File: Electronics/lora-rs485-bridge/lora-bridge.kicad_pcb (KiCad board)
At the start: 2 copper layers, 53 x 94 mm, 39 parts, among them J1 battery, J2 ANT, J3 i2c, J4 rs485, J9 USB micro, Q7 Q_PMOS_GSD, SW1 SW_Test, SW2 SW_Reset, U1 SN65HVD72, U2 ATSAMD21G18A-AUT, U3 RFM95W-868S2, U4 MCP1810T-33I_OT, Y1 32.768

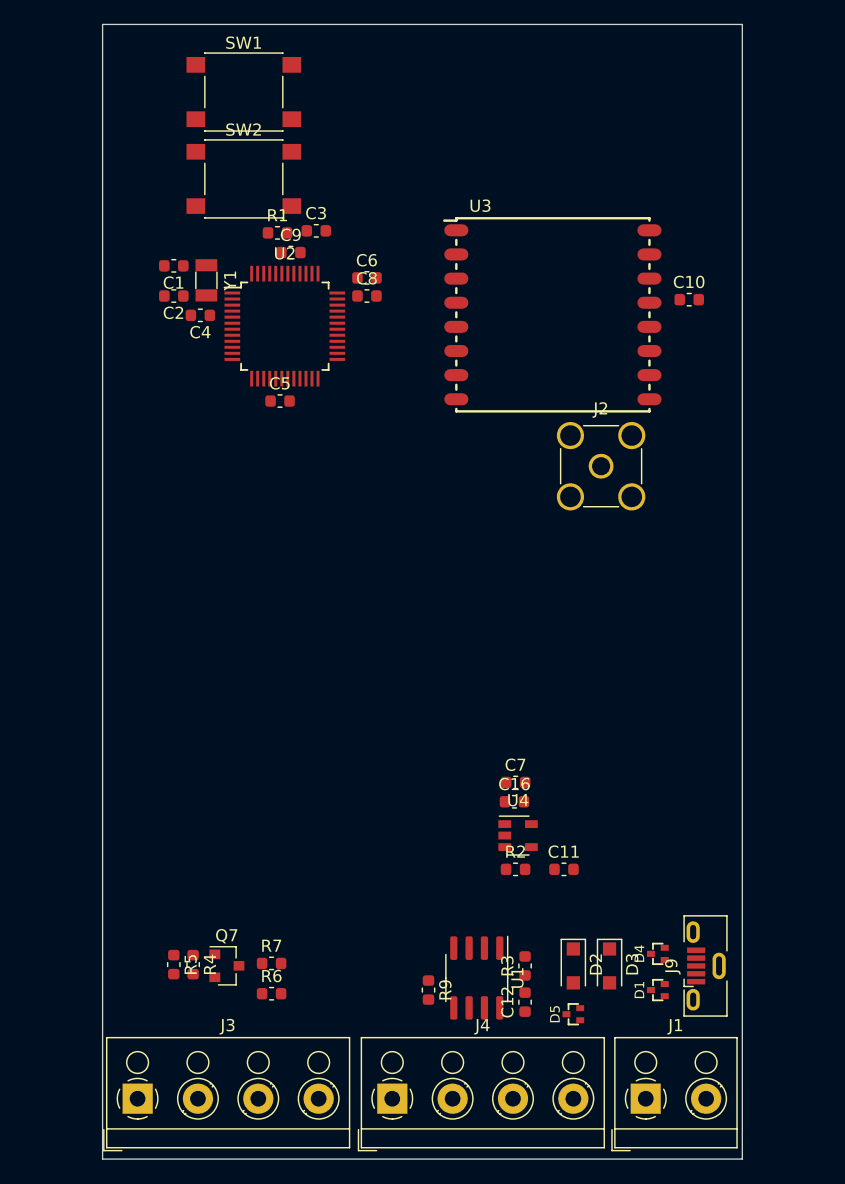
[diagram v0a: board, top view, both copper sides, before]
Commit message: Add ESD protection to i2c lines, change VIN TVS diode to higher voltage, add series resistors to SPI lines, compress the PCB to be at width of typical 4xAA battery holder
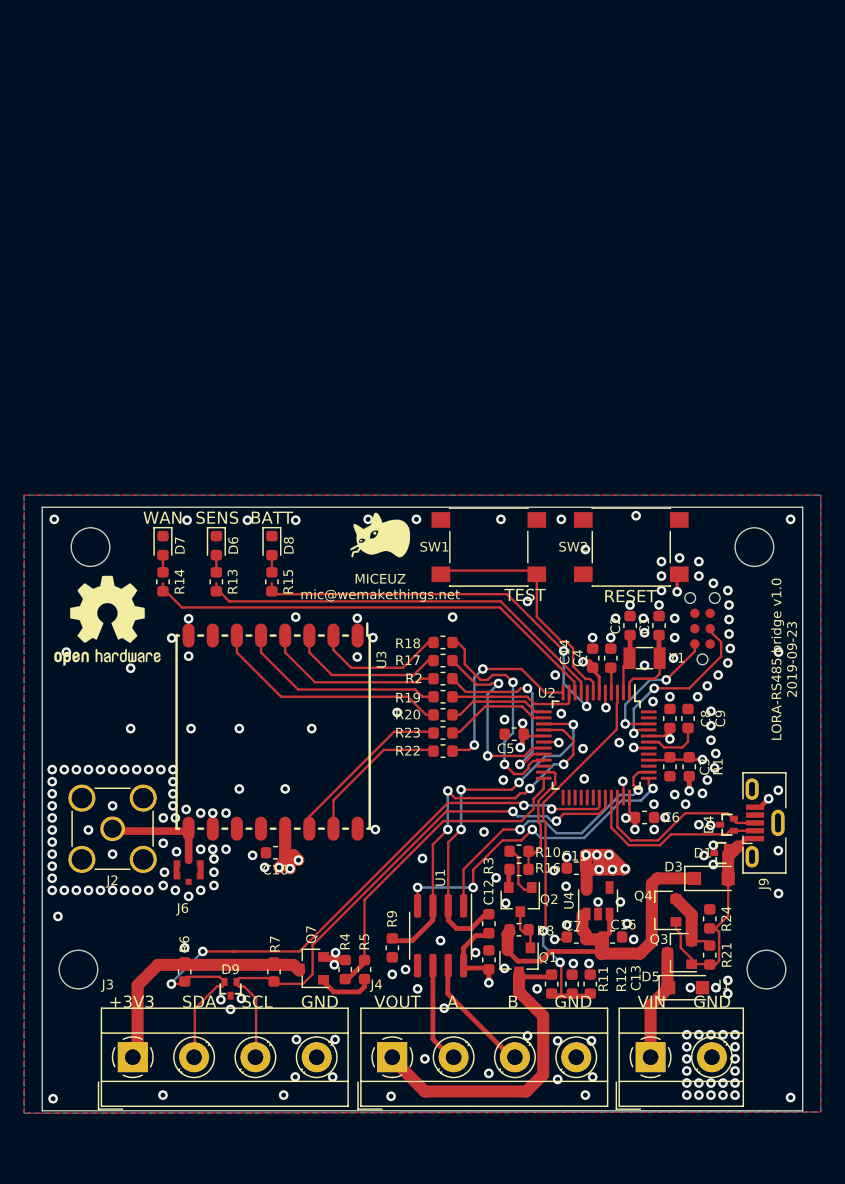
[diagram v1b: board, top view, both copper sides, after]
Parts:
- removed D2: D_Schottky, Diode_SMD:D_SOD-123F
- added C13: 1u, Capacitor_SMD:C_0603_1608Metric, F.Cu at (130.4, 132.5)
- added C14: 1u, Capacitor_SMD:C_0603_1608Metric, F.Cu at (130.6, 105.5)
- added D6: LED, LED_SMD:LED_0603_1608Metric, F.Cu at (99.4, 96.2)
- added D7: LED, LED_SMD:LED_0603_1608Metric, F.Cu at (95.0, 96.2)
- added D8: LED, LED_SMD:LED_0603_1608Metric, F.Cu at (104.0, 96.2)
- added D9: D_TVS_x2_AAC, miceuz-lib:SC89, F.Cu at (100.6, 132.9)
- added G***: LOGO, miceuz-lib:catnip, F.Cu at (113.0, 95.3)
- added H1: MountingHole, Mounting_Holes:MountingHole_3.2mm_M3_DIN965, F.Cu at (144.0, 96.3)
- added H2: MountingHole, Mounting_Holes:MountingHole_3.2mm_M3_DIN965, F.Cu at (145.0, 131.3)
- added H3: MountingHole, Mounting_Holes:MountingHole_3.2mm_M3_DIN965, F.Cu at (89.0, 96.3)
- added H4: MountingHole, Mounting_Holes:MountingHole_3.2mm_M3_DIN965, F.Cu at (88.0, 131.3)
- added J5: SWD, miceuz-lib:TC2030-MCP-NL, F.Cu at (139.7, 105.6)
- added J6: ANT, miceuz-lib:U.FL_TEConnectivity_2334884_1, F.Cu at (97.1, 123.0)
- added Q1: Q_PMOS_GSD, Package_TO_SOT_SMD:SOT-23, F.Cu at (124.5, 130.5)
- added Q2: Q_NMOS_GSD, Package_TO_SOT_SMD:SOT-23, F.Cu at (124.6, 125.5)
- added Q3: Q_PMOS_GSD, Package_TO_SOT_SMD:SOT-23, F.Cu at (137.8, 129.9)
- added Q4: Q_PMOS_GSD, Package_TO_SOT_SMD:SOT-23, F.Cu at (136.5, 126.4)
- added R10: 150, Resistor_SMD:R_0603_1608Metric, F.Cu at (124.5, 121.5)
- added R11: 10k, Resistor_SMD:R_0603_1608Metric, F.Cu at (127.2, 132.5)
- added R12: 10k, Resistor_SMD:R_0603_1608Metric, F.Cu at (128.9, 132.5)
- added R13: 10k, Resistor_SMD:R_0603_1608Metric, F.Cu at (99.4, 99.2)
- added R14: 10k, Resistor_SMD:R_0603_1608Metric, F.Cu at (95.0, 99.2)
- added R15: 10k, Resistor_SMD:R_0603_1608Metric, F.Cu at (104.0, 99.2)
- added R16: 1M, Resistor_SMD:R_0603_1608Metric, F.Cu at (124.5, 123.0)
- added R17: 150, Resistor_SMD:R_0603_1608Metric, F.Cu at (118.2, 105.7)
- added R18: 150, Resistor_SMD:R_0603_1608Metric, F.Cu at (118.2, 104.2)
- added R19: 150, Resistor_SMD:R_0603_1608Metric, F.Cu at (118.2, 108.7)
- added R20: 150, Resistor_SMD:R_0603_1608Metric, F.Cu at (118.2, 110.2)
- added R21: 1M, Resistor_SMD:R_0603_1608Metric, F.Cu at (140.3, 130.1)
- added R22: 150, Resistor_SMD:R_0603_1608Metric, F.Cu at (118.2, 113.2)
- added R23: 150, Resistor_SMD:R_0603_1608Metric, F.Cu at (118.2, 111.7)
- added R24: 150, Resistor_SMD:R_0603_1608Metric, F.Cu at (140.3, 127.1)
- added R8: 1M, Resistor_SMD:R_0603_1608Metric, F.Cu at (124.5, 128.0)
- added REF***: OSHW-Logo2_9.8x8mm_SilkScreen, Symbols:OSHW-Logo2_9.8x8mm_SilkScreen, F.Cu at (90.4, 102.4)
- D5: value D_TVS_x2_AAC -> D_TVS; footprint miceuz-lib:SC89 -> Diode_SMD:D_SOD-123F
- J1: footprint TerminalBlock_RND:TerminalBlock_RND_205-00001_Pitch5.00mm -> TerminalBlock_MetzConnect:TerminalBlock_MetzConnect_Type101_RT01602HBWC_Pitch5.08mm
- J3, J4: footprint TerminalBlock_RND:TerminalBlock_RND_205-00003_Pitch5.00mm -> TerminalBlock_MetzConnect:TerminalBlock_MetzConnect_Type101_RT01604HBWC_Pitch5.08mm
- R2: value 0 -> 150
- U4: value MCP1810T-33I_OT -> NCP718; footprint Package_TO_SOT_SMD:SOT-23-5 -> TO_SOT_Packages_SMD:SOT-23-5
- moved C10 57.2 mm to (104.3, 121.6), turned to 180 degrees
- moved R1 55.9 mm to (138.6, 114.5), turned to 90 degrees
- moved C3 53.2 mm to (137.0, 114.5), turned to -90 degrees
- moved C9 50.7 mm to (138.5, 110.5), turned to 90 degrees
- moved J2 50.4 mm to (90.8, 119.6), turned to -90 degrees
- moved C6 50.3 mm to (134.9, 118.7)
- moved C1 50.0 mm to (136.1, 102.8), turned to 90 degrees
- moved Y1 47.9 mm to (134.9, 105.5), turned to 180 degrees
- moved C2 46.6 mm to (133.7, 102.8), turned to 90 degrees
- moved C4 44.3 mm to (132.1, 105.5), turned to 90 degrees
- moved SW2 44.3 mm to (133.8, 96.3)
- moved U2 43.2 mm to (130.9, 112.7), turned to -90 degrees
- moved C8 43.1 mm to (137.0, 110.5), turned to 90 degrees
- moved SW1 42.8 mm to (122.0, 96.3)
- moved U3 34.6 mm to (111.1, 103.6), turned to -90 degrees
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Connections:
- C11 pad 1: Net-(C11-Pad1) -> +3V3
- D5 pad 2: /VIN -> GND
- J2 pad 1: GND -> /ANTENNA
- J2 pad 2: /ANTENNA -> GND
- J3 pad 2: /SCL_OUT -> /I2C_SDA
- J3 pad 3: /SDA_OUT -> /I2C_SCL
- J4 pad 1: +BATT -> /VOUT_1
- R2 pad 1: +3V3 -> Net-(R2-Pad1)
- R2 pad 2: Net-(C11-Pad1) -> /RFM_SCK
- U2 pad 10: Net-(U2-Pad10) -> /LED2
- U2 pad 15: Net-(U2-Pad15) -> /~RS485_RE
- U2 pad 16: Net-(U2-Pad16) -> /RS485_DE
- U2 pad 23: Net-(U2-Pad23) -> /RS485_ENABLE
- U2 pad 24: Net-(U2-Pad24) -> /~I2C_ENABLE
- U2 pad 3: Net-(U2-Pad3) -> /BATT_MON
- U2 pad 7: Net-(U2-Pad7) -> Net-(SW1-Pad2)
- U2 pad 8: Net-(U2-Pad8) -> /LED3
- U2 pad 9: Net-(U2-Pad9) -> /LED1
- U3 pad 14: /RFM_IRQ -> Net-(R23-Pad2)
- U3 pad 15: /DIO01 -> Net-(R22-Pad2)
- U3 pad 2: /RFM_MISO -> Net-(R18-Pad1)
- U3 pad 3: /RFM_MOSI -> Net-(R17-Pad1)
- U3 pad 4: /RFM_SCK -> Net-(R2-Pad1)
- U3 pad 5: /RFM_NSS -> Net-(R19-Pad1)
- U3 pad 6: /RFM_RST -> Net-(R20-Pad1)
- U4 pad 2: +BATT -> GND
- U4 pad 3: +3V3 -> +BATT
- U4 pad 5: GND -> +3V3
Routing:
- net /I2C_SDA: track 0.00 -> 55.9 mm, vias 0 -> 4
- net /I2C_SCL: track 0.00 -> 47.6 mm, vias 0 -> 2
- net +3V3: track 0.00 -> 42.5 mm, vias 0 -> 19
- net /LED2: track 0.00 -> 38.6 mm
- net /LED1: track 0.00 -> 34.8 mm
- net /LED3: track 0.00 -> 33.3 mm, vias 0 -> 2
- net +BATT: track 0.00 -> 32.1 mm
- net /BATT_MON: track 0.00 -> 31.5 mm, vias 0 -> 2
- net /RS485_DE: track 0.00 -> 31.4 mm, vias 0 -> 4
- net /~RS485_RE: track 0.00 -> 30.2 mm, vias 0 -> 4
- net /~I2C_ENABLE: track 0.00 -> 27.5 mm
- net /TX: track 0.00 -> 27.1 mm, vias 0 -> 4
- net /VOUT_1: track 0.00 -> 26.1 mm
- net /RX: track 0.00 -> 23.9 mm, vias 0 -> 2
- net /~MCU_RST: track 0.00 -> 21.0 mm, vias 0 -> 2
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- added copper zone on In2.Cu, net +3V3
- added copper zone on B.Cu, net GND
- added copper zone on F.Cu, net GND
- added copper zone on In1.Cu, net GND
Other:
- board size 53 x 94 mm -> 63 x 50 mm
- copper layers 2 -> 4
- board text added: "+3V3"
- board text added: "A"
- board text added: "B"
- board text added: "BATT"
- board text added: "GND"
- board text added: "LORA-RS485 bridge v1.0 2019-09-23"
- board text added: "MICEUZ mic@wemakethings.net"
- board text added: "Output current: 100mA max"
- board text added: "Output current: 1A max"
- board text added: "RESET"
- board text added: "SCL"
- board text added: "SDA"
- board text added: "SENS"
- board text added: "TEST"
- board text added: "VIN"
- board text added: "VIN 4 - 12V"
- board text added: "VOUT"
- board text added: "WAN"

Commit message: Add power input PTC fuse
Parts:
- removed J6: ANT, miceuz-lib:U.FL_TEConnectivity_2334884_1
- added REF***: WEEE-Logo_4.2x6mm_SilkScreen, Symbols:WEEE-Logo_4.2x6mm_SilkScreen, B.Cu at (121.9, 119.9)
- added REF***: RoHS-Logo_6mm_SilkScreen, Symbols:RoHS-Logo_6mm_SilkScreen, B.Cu at (135.7, 119.8)
- added REF***: ESD-Logo_6.6x6mm_SilkScreen, Symbols:ESD-Logo_6.6x6mm_SilkScreen, B.Cu at (133.1, 111.8)
- added REF***: CE-Logo_8.5x6mm_SilkScreen, Symbols:CE-Logo_8.5x6mm_SilkScreen, B.Cu at (142.8, 112.1)
- added TH1: Thermistor_PTC, Fuse:Fuse_1206_3216Metric, F.Cu at (133.7, 132.8)
- J2: footprint Connector_Coaxial:SMA_Amphenol_901-144_Vertical -> Connector_Coaxial:SMA_Amphenol_132289_EdgeMount
- moved J2 3.03 mm to (87.8, 119.8), turned to 180 degrees
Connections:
- D5 pad 1: /VIN -> Net-(D5-Pad1)
- Q3 pad 3: /VIN -> Net-(D5-Pad1)
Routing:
- net Net-(D5-Pad1): track 0.00 -> 4.74 mm
- net /VIN: track 9.33 -> 7.05 mm
- net /ANTENNA: track 8.82 -> 9.34 mm
- net GND: vias 218 -> 220
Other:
- board text added: "LORA-RS485 bridge v1.1 2019-11-05"
- board text added: "Manufacturer: Albertas Mickėnas Mindaugo 25 03011 Vilnius Lithuania"
- board text removed: "LORA-RS485 bridge v1.0 2019-09-23"

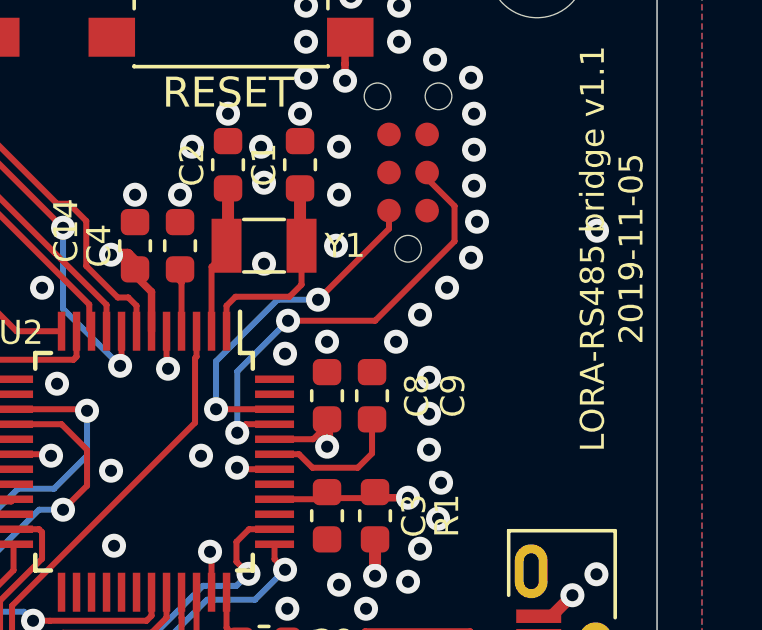
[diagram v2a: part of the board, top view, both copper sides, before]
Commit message: Add pullup to SWDCLK for better stability. Change reset pullup value to 1k
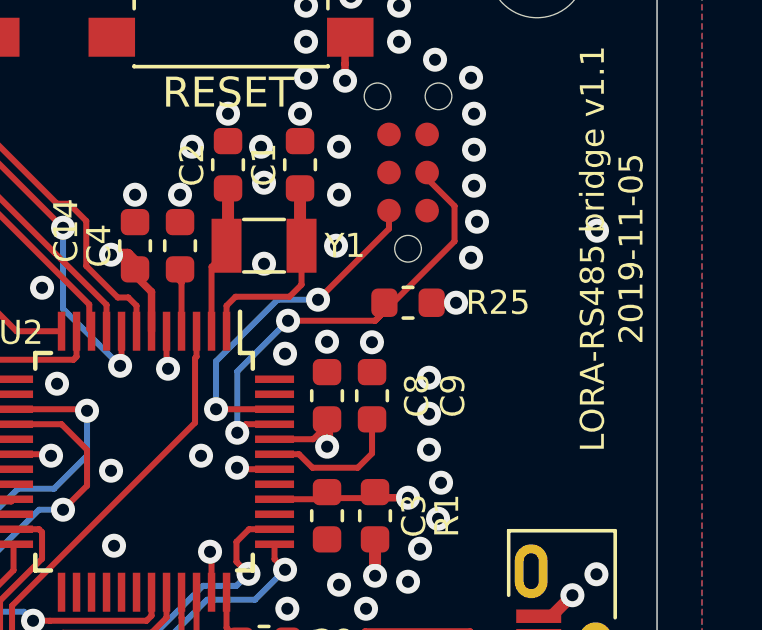
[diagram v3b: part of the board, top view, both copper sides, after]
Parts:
- added R25: 1k, Resistor_SMD:R_0603_1608Metric, F.Cu at (139.7, 107.4)
- R1: value 10k -> 1k
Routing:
- net +3V3: track 42.5 -> 43.3 mm, vias 19 -> 20
- net /SWD_CLK: track 14.9 -> 15.6 mm
- net GND: vias 220 -> 218

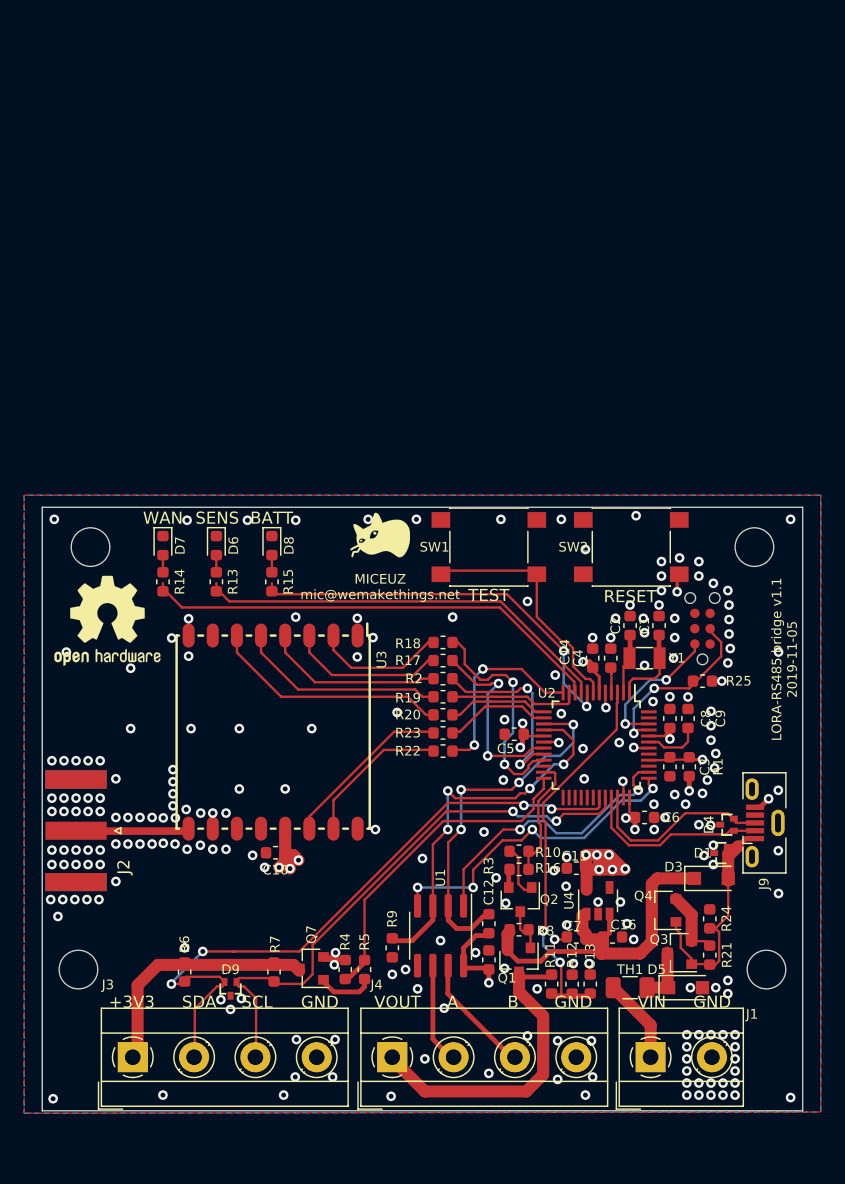
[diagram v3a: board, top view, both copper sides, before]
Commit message: Update D3 to silicone diode as schottky leaks as hell; Add D2 to protect gates of mosfets; Remove series resistors from RFM95 interface, add pullups/downs for better sleep stability; Unify resistor values across the board; Bump version number to v1.2
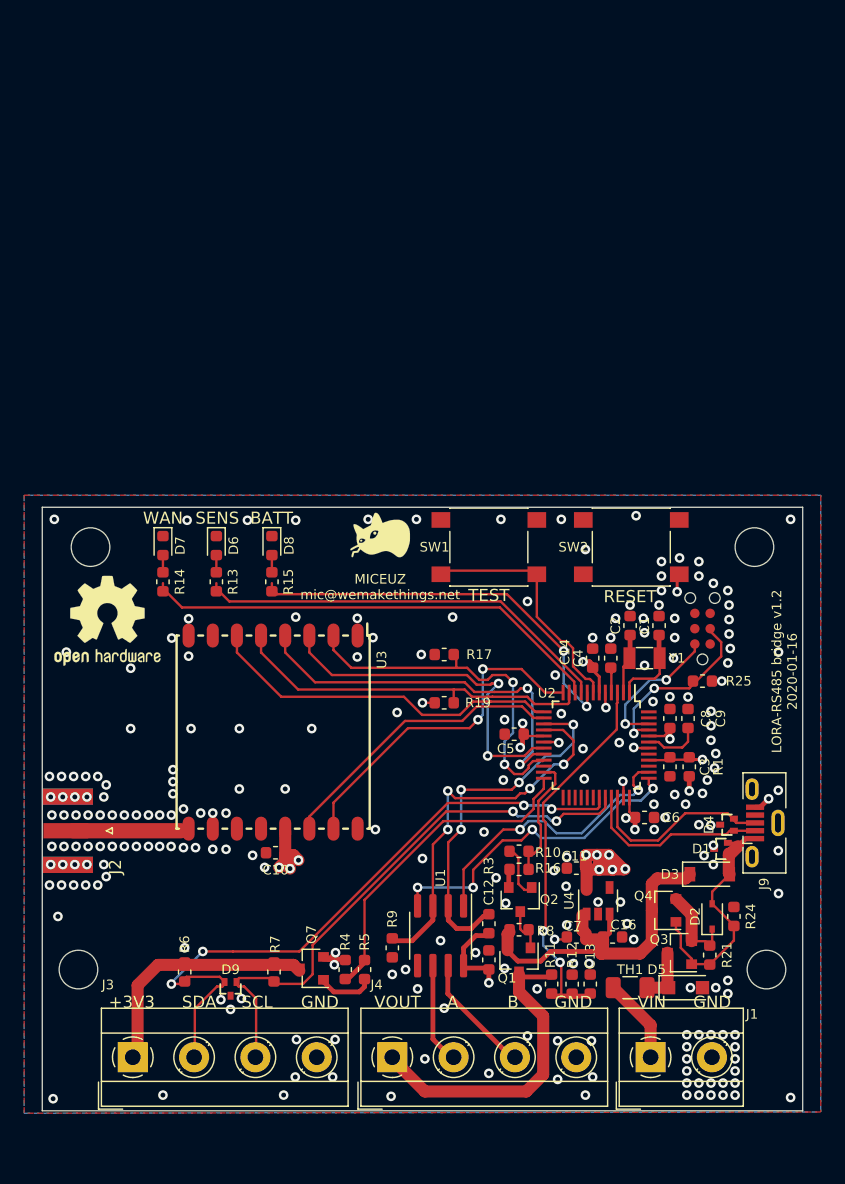
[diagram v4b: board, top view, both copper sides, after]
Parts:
- removed R18, R2, R20, R22, R23: 150, Resistor_SMD:R_0603_1608Metric
- added D2: 7.6V, Diode_SMD:D_SOD-323, F.Cu at (140.5, 126.9)
- D3: value D_Schottky -> 1N4148; footprint Diode_SMD:D_SOD-123F -> Diode_SMD:D_SOD-123
- J2: footprint Connector_Coaxial:SMA_Amphenol_132289_EdgeMount -> miceuz-lib:SMA_6.35_EdgeMount
- moved R24 2.01 mm to (142.3, 126.9)
- moved J2 0.70 mm to (87.1, 119.8)
- moved R17 0.51 mm to (118.3, 105.2), turned to 180 degrees
- moved R19 0.51 mm to (118.3, 109.2)
- moved D3 0.37 mm to (140.3, 123.4)
- moved D1 0.35 mm to (141.2, 121.3)
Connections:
- R17 pad 1: Net-(R17-Pad1) -> /RFM_MISO
- R17 pad 2: /RFM_MOSI -> GND
- R19 pad 1: Net-(R19-Pad1) -> +3V3
- U3 pad 14: Net-(R23-Pad2) -> /RFM_IRQ
- U3 pad 15: Net-(R22-Pad2) -> /DIO01
- U3 pad 2: Net-(R18-Pad1) -> /RFM_MISO
- U3 pad 3: Net-(R17-Pad1) -> /RFM_MOSI
- U3 pad 4: Net-(R2-Pad1) -> /RFM_SCK
- U3 pad 5: Net-(R19-Pad1) -> /RFM_NSS
- U3 pad 6: Net-(R20-Pad1) -> /RFM_RST
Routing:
- net /RFM_RST: track 8.37 -> 29.6 mm
- net /RFM_NSS: track 10.8 -> 30.5 mm
- net Net-(R20-Pad1): track 19.6 -> 0.00 mm
- net Net-(R19-Pad1): track 17.0 -> 0.00 mm
- net /RFM_IRQ: track 8.83 -> 24.8 mm
- net /RFM_SCK: track 16.0 -> 32.0 mm
- net Net-(R2-Pad1): track 14.6 -> 0.00 mm
- net Net-(R23-Pad2): track 14.4 -> 0.00 mm
- net /RFM_MOSI: track 16.0 -> 29.3 mm
- net /DIO01: track 16.0 -> 29.0 mm
- net Net-(R17-Pad1): track 12.8 -> 0.00 mm
- net Net-(R22-Pad2): track 12.6 -> 0.00 mm
- net /RFM_MISO: track 18.7 -> 30.0 mm
- net Net-(R18-Pad1): track 11.0 -> 0.00 mm
- net Net-(D2-Pad1): track 5.69 -> 7.13 mm
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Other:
- net class antenna added: clearance 0.25, trace_width 1.27, via_dia 0.8, via_drill 0.4
- board text added: "LORA-RS485 bridge v1.2 2020-01-16"
- board text removed: "LORA-RS485 bridge v1.1 2019-11-05"
